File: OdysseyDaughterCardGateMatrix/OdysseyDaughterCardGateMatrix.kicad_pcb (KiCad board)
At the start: 2 copper layers, 37.6 x 46.6 mm, 18 parts, among them J1 Conn_01x01, X1 OdysseyDaughterCard

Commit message: OdysseyDaughterCardGateMatrix: Open and close in KiCad 6, fix symbol library path
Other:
- net class Default removed

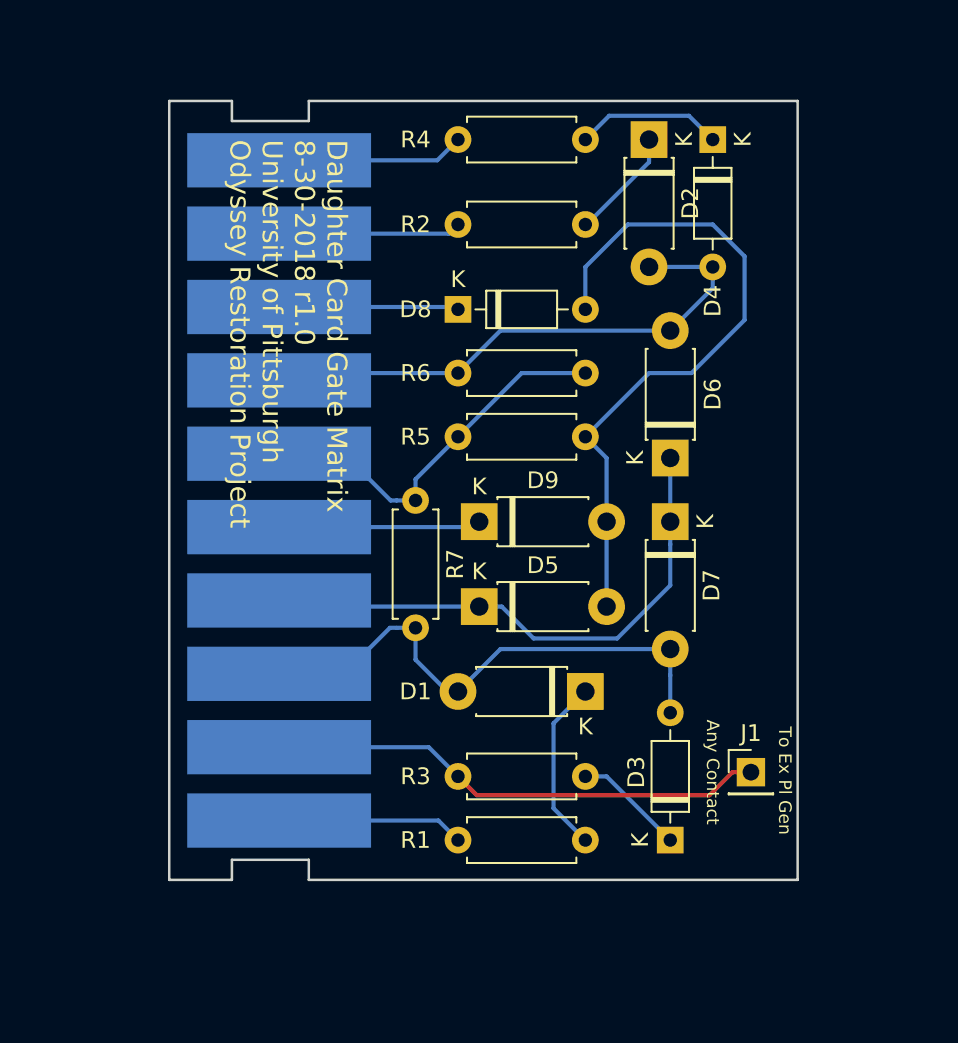
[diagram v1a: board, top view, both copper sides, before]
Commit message: OdysseyDaughterCardGateMatrix wider transistor footprint, add logo, generate pdf, images, 3d models
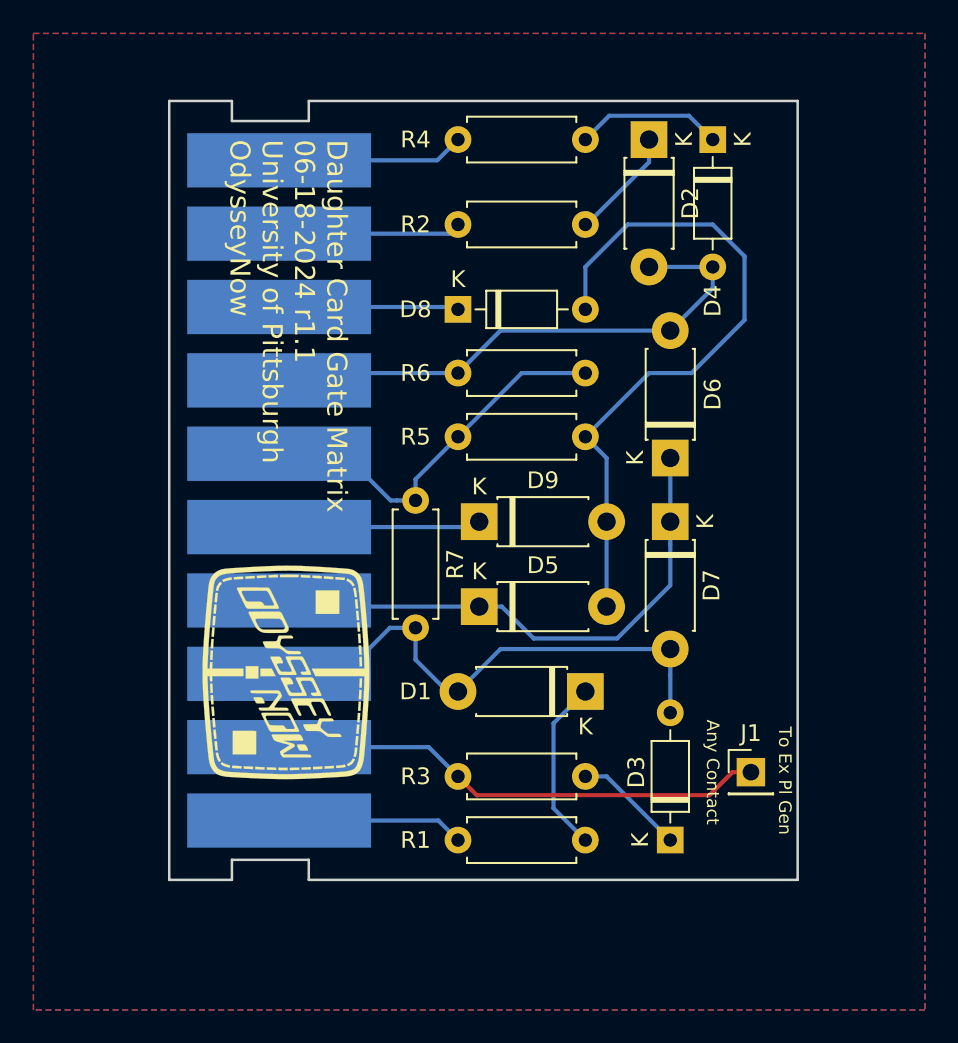
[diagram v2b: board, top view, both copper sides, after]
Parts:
- added X1: OdysseyNow_Logo, Odyssey_Daughter_Card:OdysseyNowLogo, F.Cu at (130.2, 111.6)
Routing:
- added copper zone on B.Cu, net /Card6
- added copper zone on F.Cu, net /Card6
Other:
- board text added: "Daughter Card Gate Matrix 06-18-2024 r1.1 University of Pittsburgh OdysseyNow"
- board text removed: "Daughter Card Gate Matrix 8-30-2018 r1.0 University of Pittsburgh Odyssey Restoration Project"
